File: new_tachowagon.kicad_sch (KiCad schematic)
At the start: 39 parts, among them J1 5V Buffer, J2 I2C, J3 UART, J4 Conn_02x03_Odd_Even, Q1 6N137S1TA, U1 AMS1117-3.3, U2 ESP32-S3-WROOM-1-N16R8, U901 MT2499A

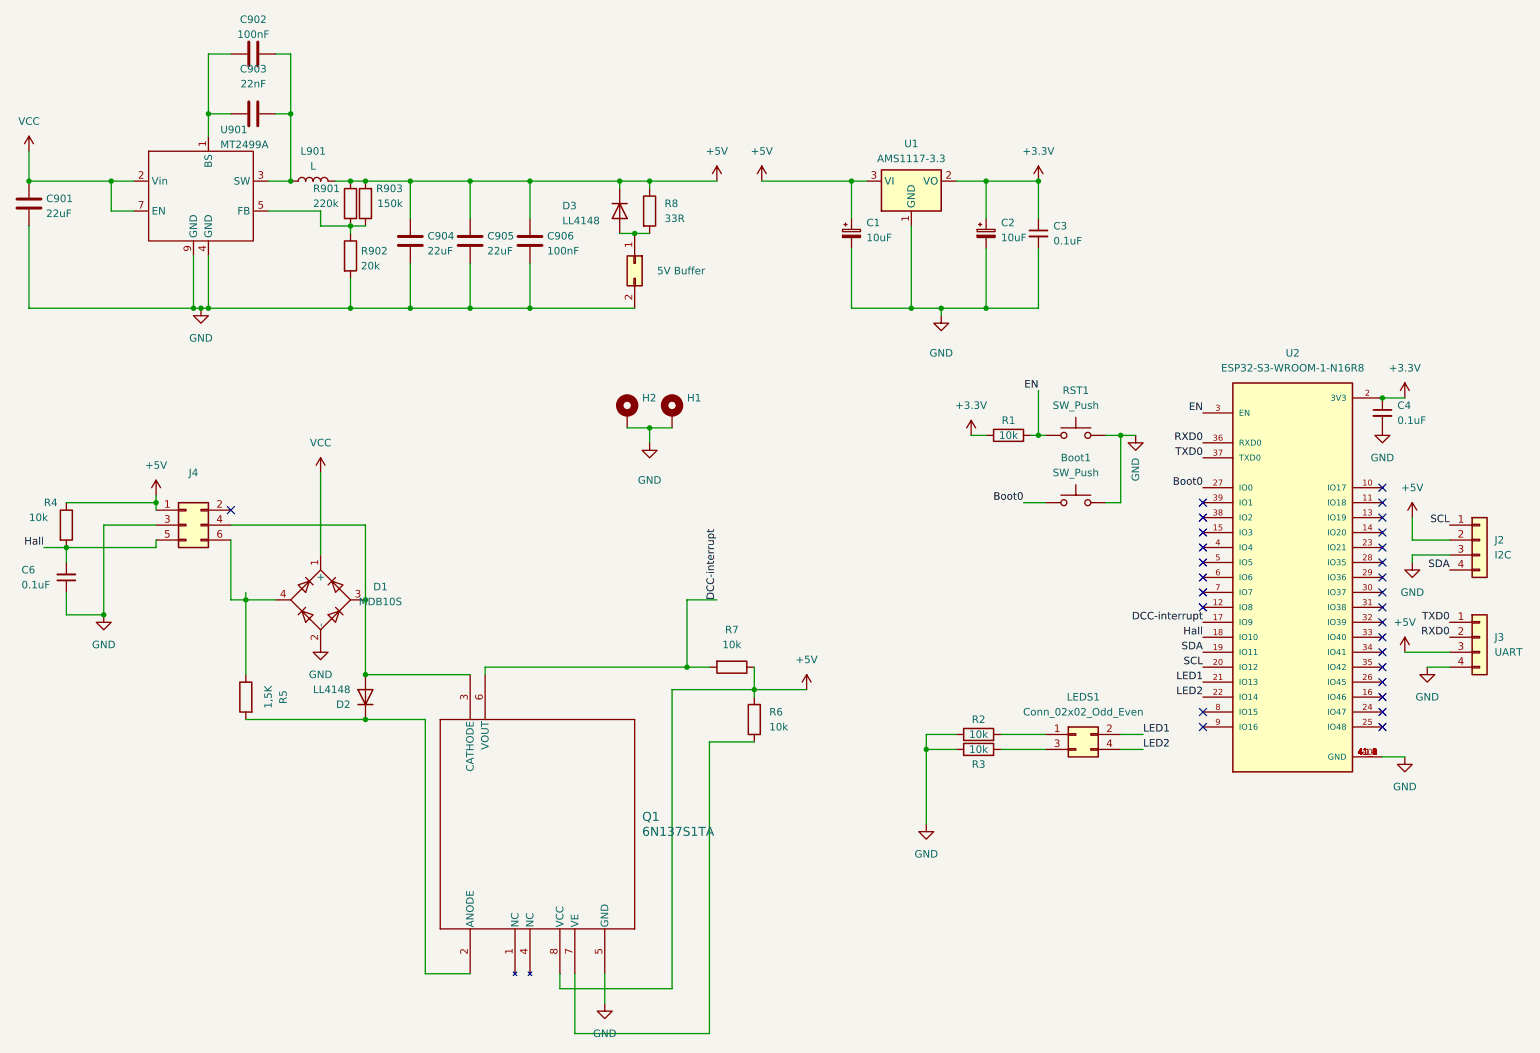
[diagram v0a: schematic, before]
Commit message: added hierachic sheets
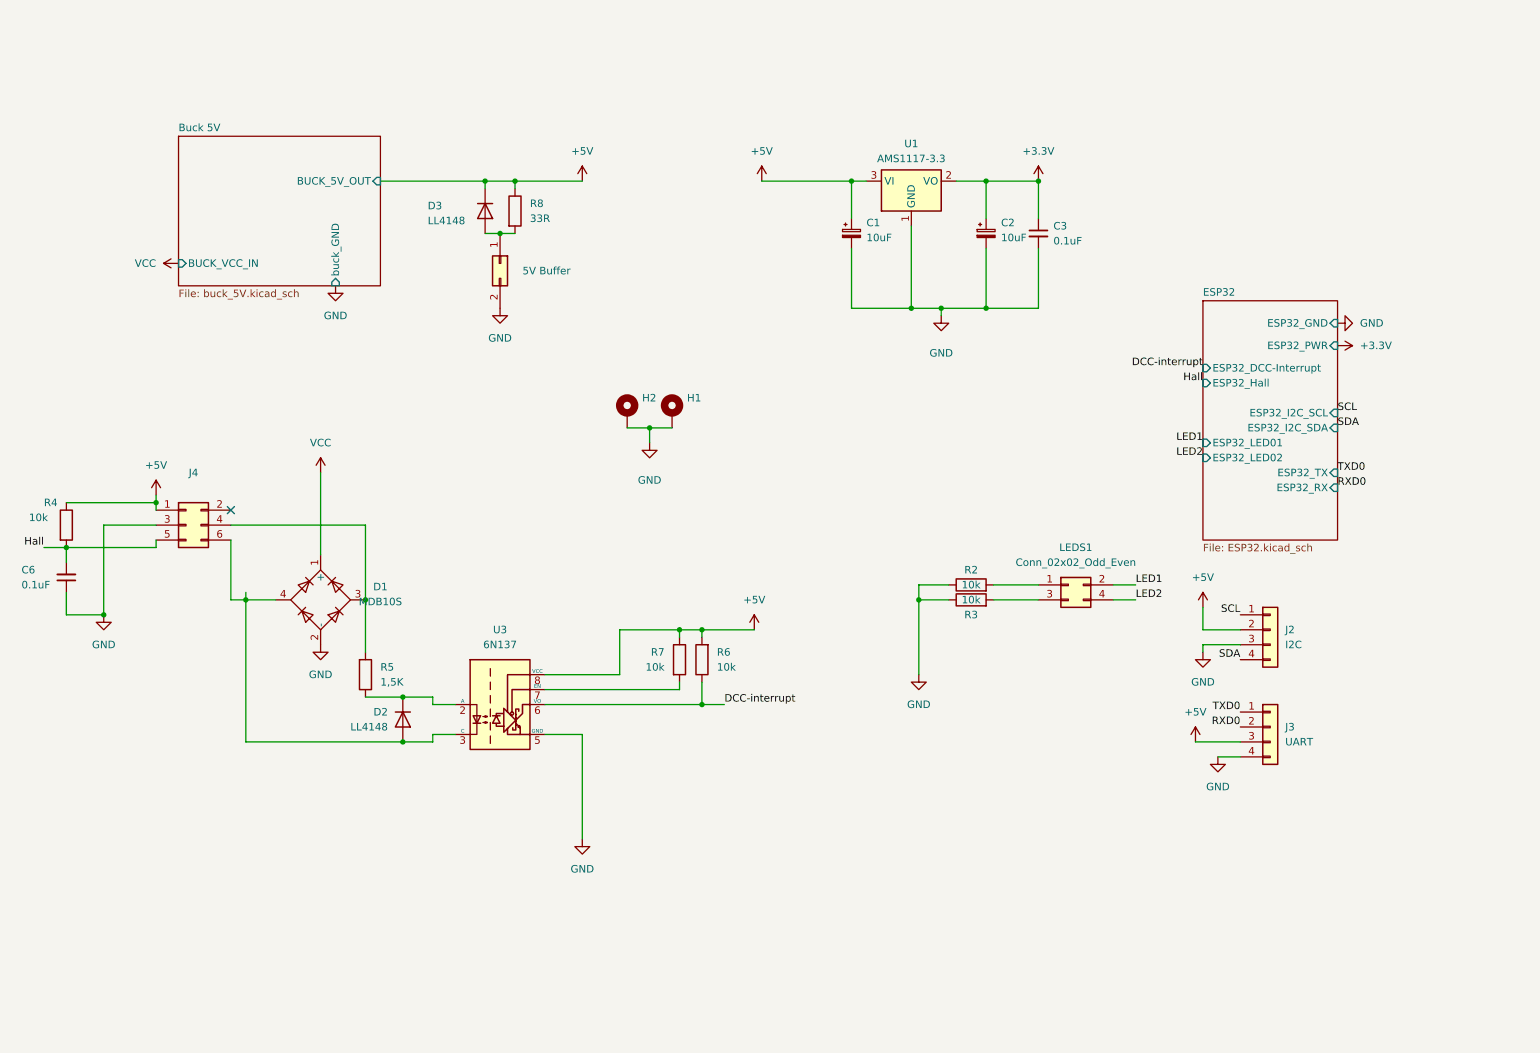
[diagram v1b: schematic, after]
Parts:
- removed Boot1, RST1: SW_Push, Button_Switch_SMD:SW_Push_1P1T_XKB_TS-1187A, symbol Switch:SW_Push
- removed C4: 0.1uF, Capacitor_SMD:C_0603_1608Metric, symbol Device:C_Small
- removed C901, C904, C905: 22uF, Capacitor_SMD:C_0603_1608Metric, symbol Device:C
- removed C902, C906: 100nF, Capacitor_SMD:C_0402_1005Metric, symbol Device:C
- removed C903: 22nF, Capacitor_SMD:C_0402_1005Metric, symbol Device:C
- removed L901: L, Inductor_SMD:L_Bourns-SRN8040_8x8.15mm, symbol Device:L
- removed Q1: 6N137S1TA, 6N137S1:6N137S1TA_EVE, symbol 6N137S1(TA):6N137S1TA
- removed R1: 10k, Resistor_SMD:R_1206_3216Metric, symbol Device:R
- removed R901: 220k, Resistor_SMD:R_0603_1608Metric, symbol Device:R
- removed R902: 20k, Resistor_SMD:R_0603_1608Metric, symbol Device:R
- removed R903: 150k, Resistor_SMD:R_0603_1608Metric, symbol Device:R
- removed U2: ESP32-S3-WROOM-1-N16R8, ESP32-S3-WROOM-1-N16R8:XCVR_ESP32-S3-WROOM-1-N16R8, symbol ESP32-S3-WROOM-1:ESP32-S3-WROOM-1-N16R8
- removed U901: MT2499A, Package_SO:TI_SO-PowerPAD-8, symbol custom_kicad_lib_sk:MT499A
- added U3: 6N137, Package_SO:SOP-8_6.605x9.655mm_P2.54mm, symbol Isolator:6N137
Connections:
- net +5V: now also U3.8 (VCC)
- net DCC-interrupt: now also R6.1, U3.6 (VO); no longer R7.2
- net GND: now also U3.5 (GND)
- net at D1.3, J4.4 (Pin_4): now also R5.2; no longer D2.2 (A)
- net at D1.4, J4.6 (Pin_6): now also D2.2 (A), U3.3 (C); no longer R5.1
- net at D2.1 (K): now also R5.1, U3.2 (A); no longer R5.2
- new net: R7.2, U3.7 (EN)
- no-connect marks 28 -> 1
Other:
- added sheet Buck 5V (buck_5V.kicad_sch)
- added sheet ESP32 (ESP32.kicad_sch)
- moved on the sheet: LEDS1, R2, R3, R6, R7
